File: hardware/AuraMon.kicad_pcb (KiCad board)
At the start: 4 copper layers, 48.2 x 95.9 mm, 118 parts, among them J1 USB_C_Receptacle_USB2.0_16P, J10 Conn_01x03, J11 Conn_01x03, J12 Conn_01x03, J13 Conn_01x03, J14 Conn_01x03, J15 Conn_01x03, J16 Conn_01x03, J17 Conn_01x03, J18 Conn_01x03, J19 Conn_01x03, J2 Conn_01x06, J20 Conn_01x03, J21 Conn_01x03, J3 Conn_01x03, J4 RJ45_Hanrun_HR911105A_Horizon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, J5 Micro_SD_Card_Det_Hirose_DM3AT, J6 1881448, J7 Conn_01x06, J8 Conn_02x02_Odd_Even, J9 Conn_01x06, SW2 SW_Push, SW3 SW_Push, U1 W25Q128JVS, U2 RP2350A, U3 MAX3485, U4 W5500, U5 AMS1117-3.3, U6 PCF8563TS, Y1 ABM8-272-T3, Y2 XO32F025000GEHE001, Y3 X321532768KGD2SI

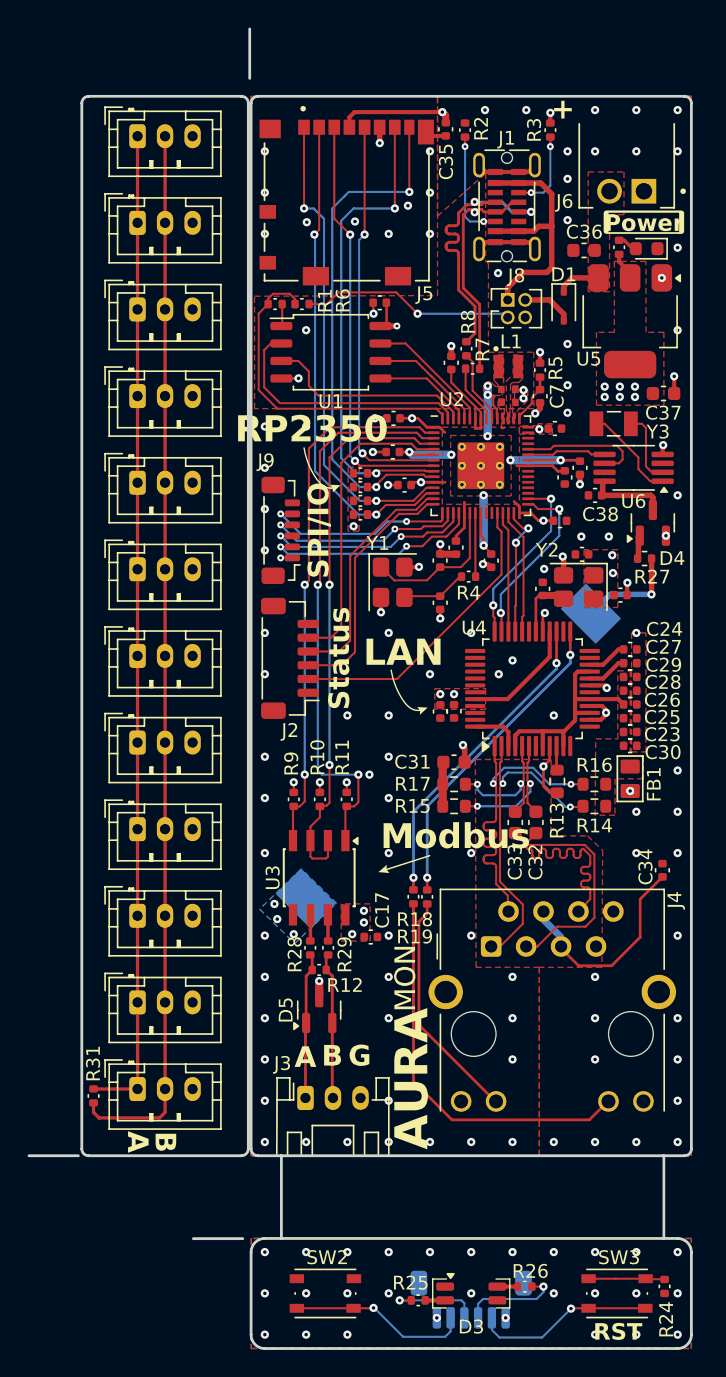
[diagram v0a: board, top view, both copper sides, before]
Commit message: fix: unavailable components
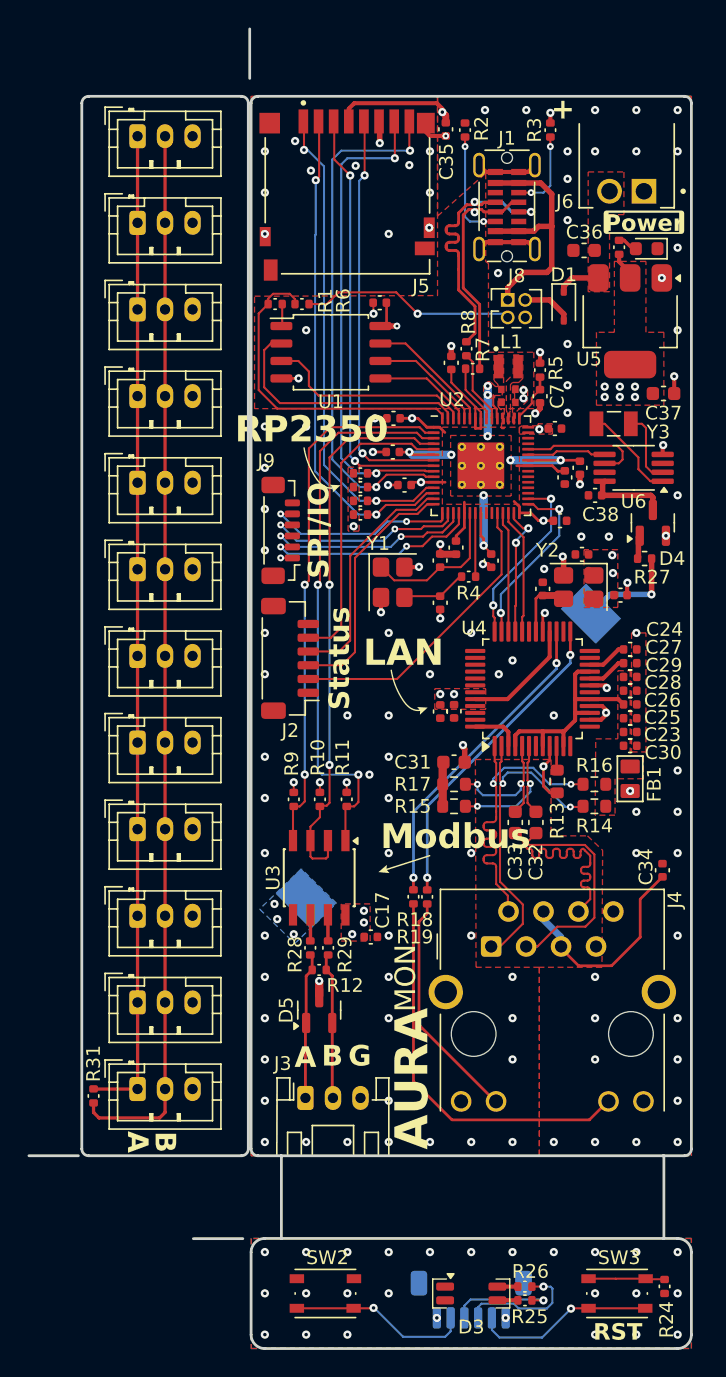
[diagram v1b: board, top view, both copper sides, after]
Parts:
- J5: footprint AuraMon:MOLEX_104031-0811 -> AuraMon:AMPHENOL_1140084168
- moved R25 7.75 mm to (107.9, 130.3), turned to 180 degrees
- moved J5 5.00 mm to (95.0, 45.5)
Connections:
- D3 pad 3: GND -> Net-(D3-A2)
- D3 pad 4: Net-(D3-A2) -> GND
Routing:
- net /Control/LED_G: track 7.37 -> 9.20 mm
- net /Control/LED_R: track 6.70 -> 7.69 mm
- net +3V3: track 49.4 -> 50.1 mm

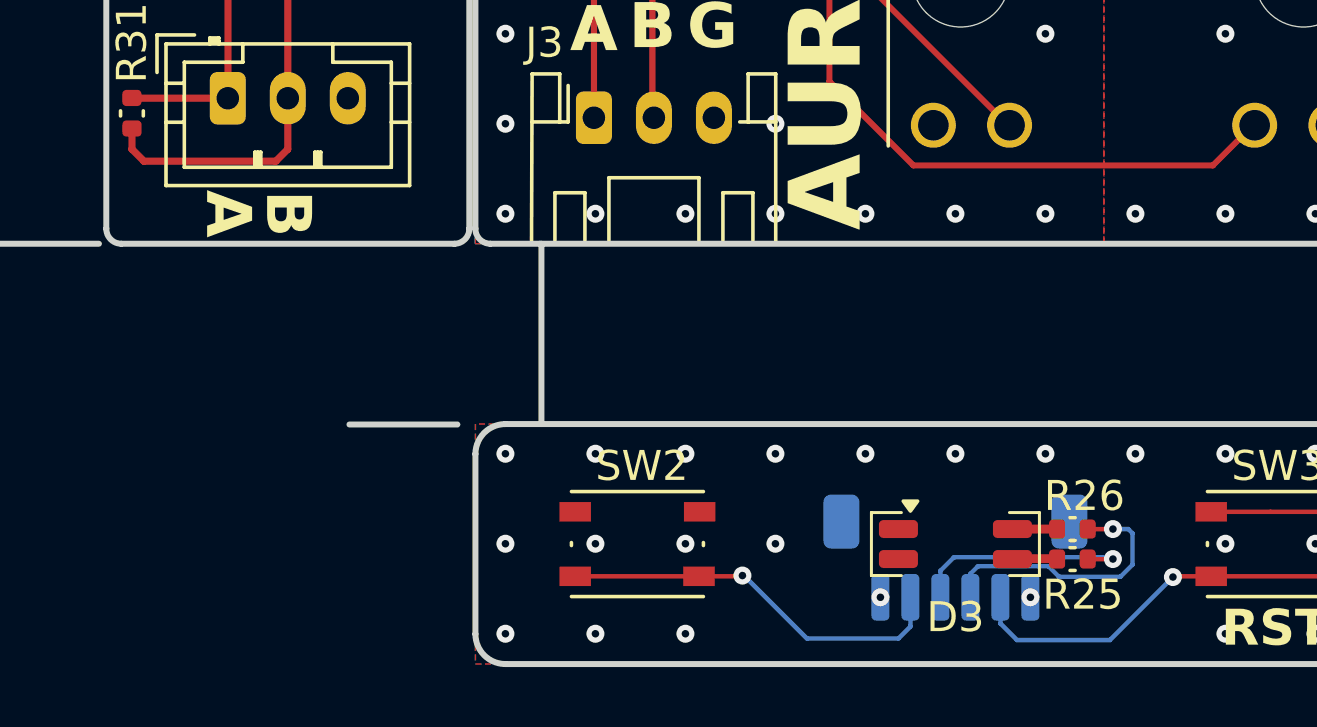
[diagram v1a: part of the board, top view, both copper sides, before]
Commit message: feat: replace status LED
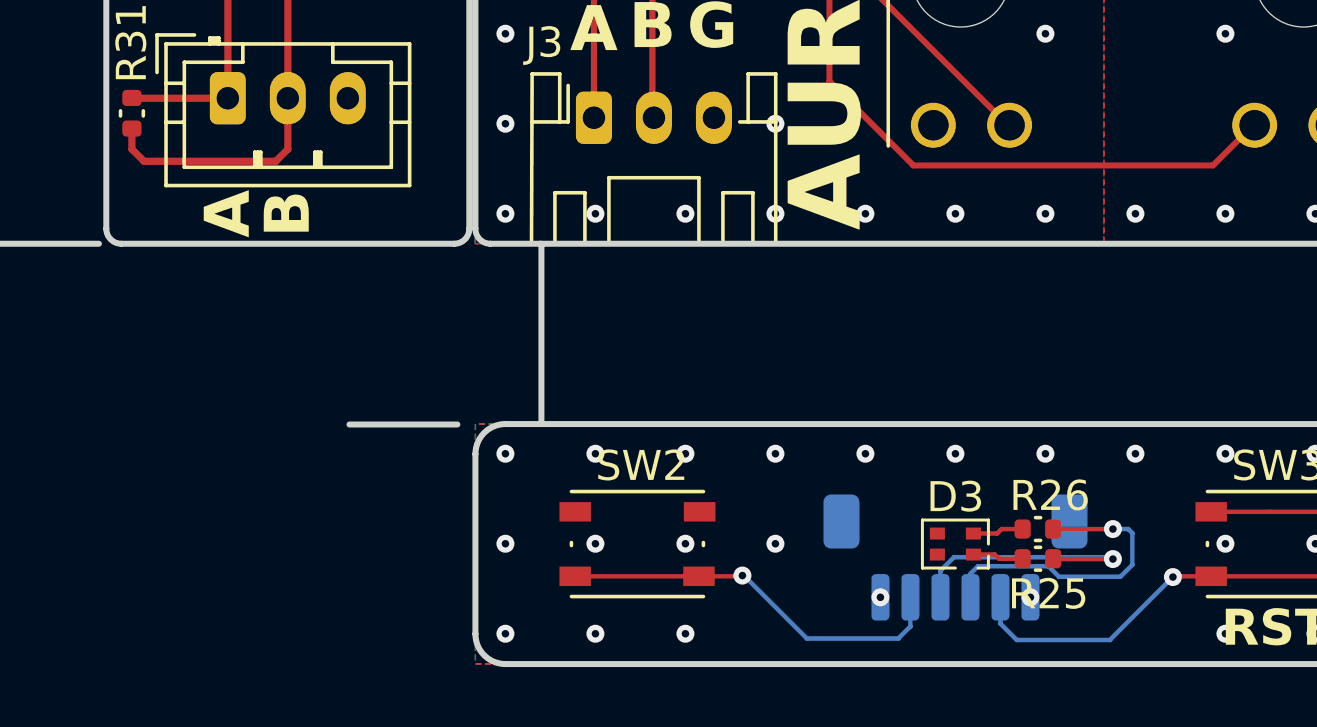
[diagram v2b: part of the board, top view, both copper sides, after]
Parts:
- D3: footprint LED_SMD:LED_LiteOn_LTST-C235KGKRKT -> LED_SMD:LED_LiteOn_LTST-C295K_1.6x0.8mm
- moved R25 1.15 mm to (106.8, 130.3)
- moved R26 1.15 mm to (106.8, 129.3)
- turned D3 to 180 degrees
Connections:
- D3 pad 1: GND -> Net-(D3-A1)
- D3 pad 3: Net-(D3-A2) (its old number) -> GND
- R25 pad 2: Net-(D3-A2) (its old number) -> Net-(D3-A1)
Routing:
- net Net-(D3-A1): track 0.00 -> 1.70 mm
- net Net-(D3-A2) (its old number): track 1.49 -> 0.00 mm
- net /Control/LED_G: track 9.20 -> 10.3 mm
- net /Control/LED_R: track 7.69 -> 8.84 mm

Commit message: fix: status LED resistor value
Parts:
- R25, R26: value 470 -> 1k

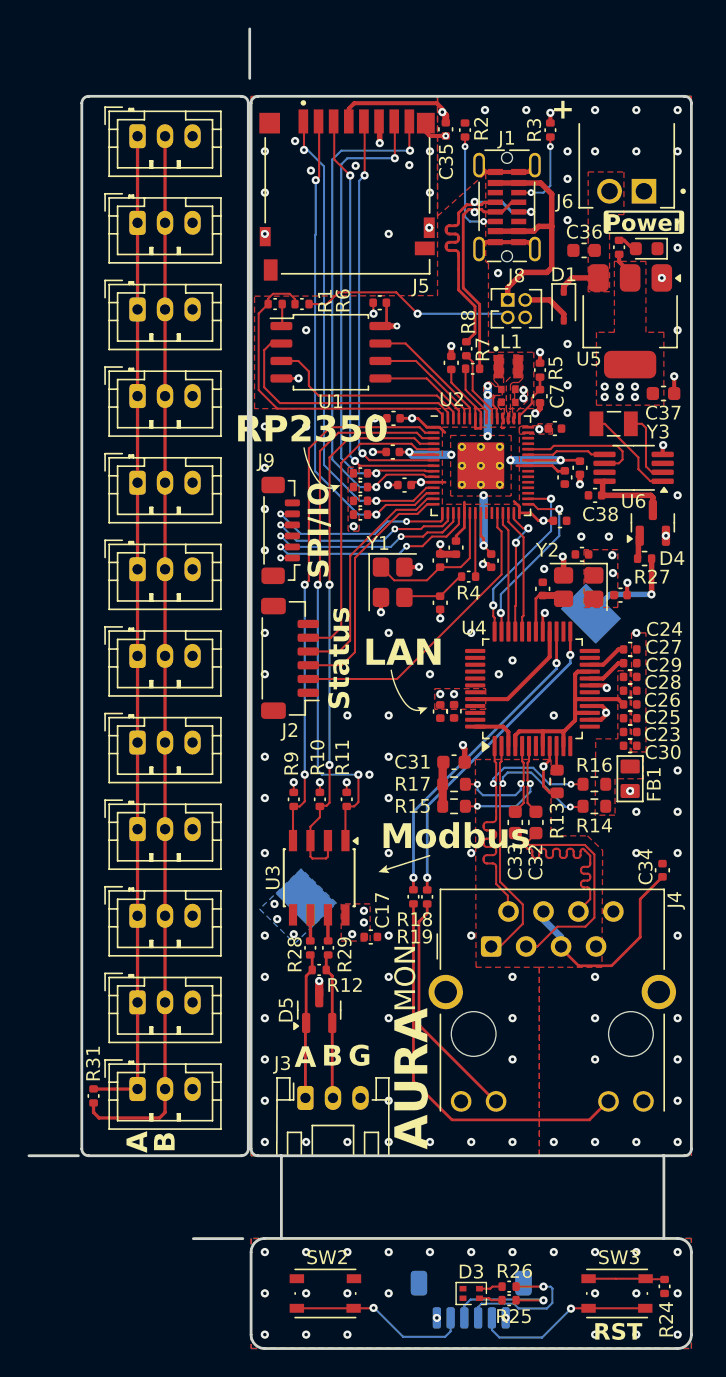
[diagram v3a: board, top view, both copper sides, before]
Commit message: feat: add SWD footprint
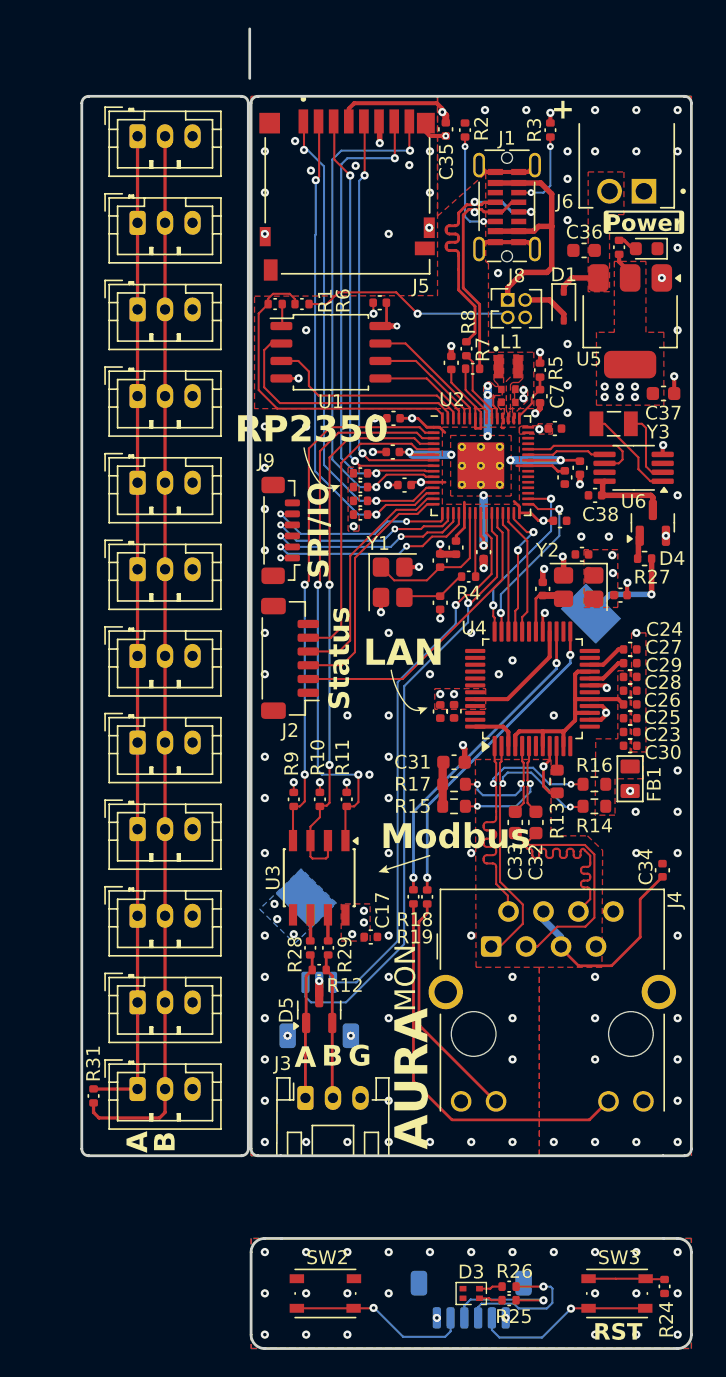
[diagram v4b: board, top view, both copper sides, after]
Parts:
- added J22: SM03B-SRSS-TB, Connector_JST:JST_SH_SM03B-SRSS-TB_1x03-1MP_P1.00mm_Horizontal, B.Cu at (93.0, 109.2)
- R25, R26: value 1k -> 470
- moved OSHW 62.2 mm to (93.1, 47.6)
- moved C8 0.83 mm to (104.9, 75.9)
- moved SS3 0.15 mm to (110.0, 111.2)
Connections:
- U2 pad 24: unconnected-(U2-SWCLK-Pad24) -> /MCU/SWCLK
- U2 pad 25: unconnected-(U2-SWD-Pad25) -> /MCU/SWD
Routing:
- net /MCU/SWD: track 0.00 -> 44.5 mm, vias 0 -> 1
- net /MCU/SWCLK: track 0.00 -> 40.2 mm, vias 0 -> 1
- net GND: track 46.1 -> 47.1 mm, vias 152 -> 154
- net +1V1: track 25.2 -> 24.4 mm
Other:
- board size 48.2 x 95.9 mm -> 44.3 x 95.9 mm
- board text added: "Debug"
